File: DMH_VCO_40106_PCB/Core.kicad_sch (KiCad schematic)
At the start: 58 parts, among them Q1 BC558, Q2 BC548, U1 40106, U2 TL074, U3 TL074, U4 TL074

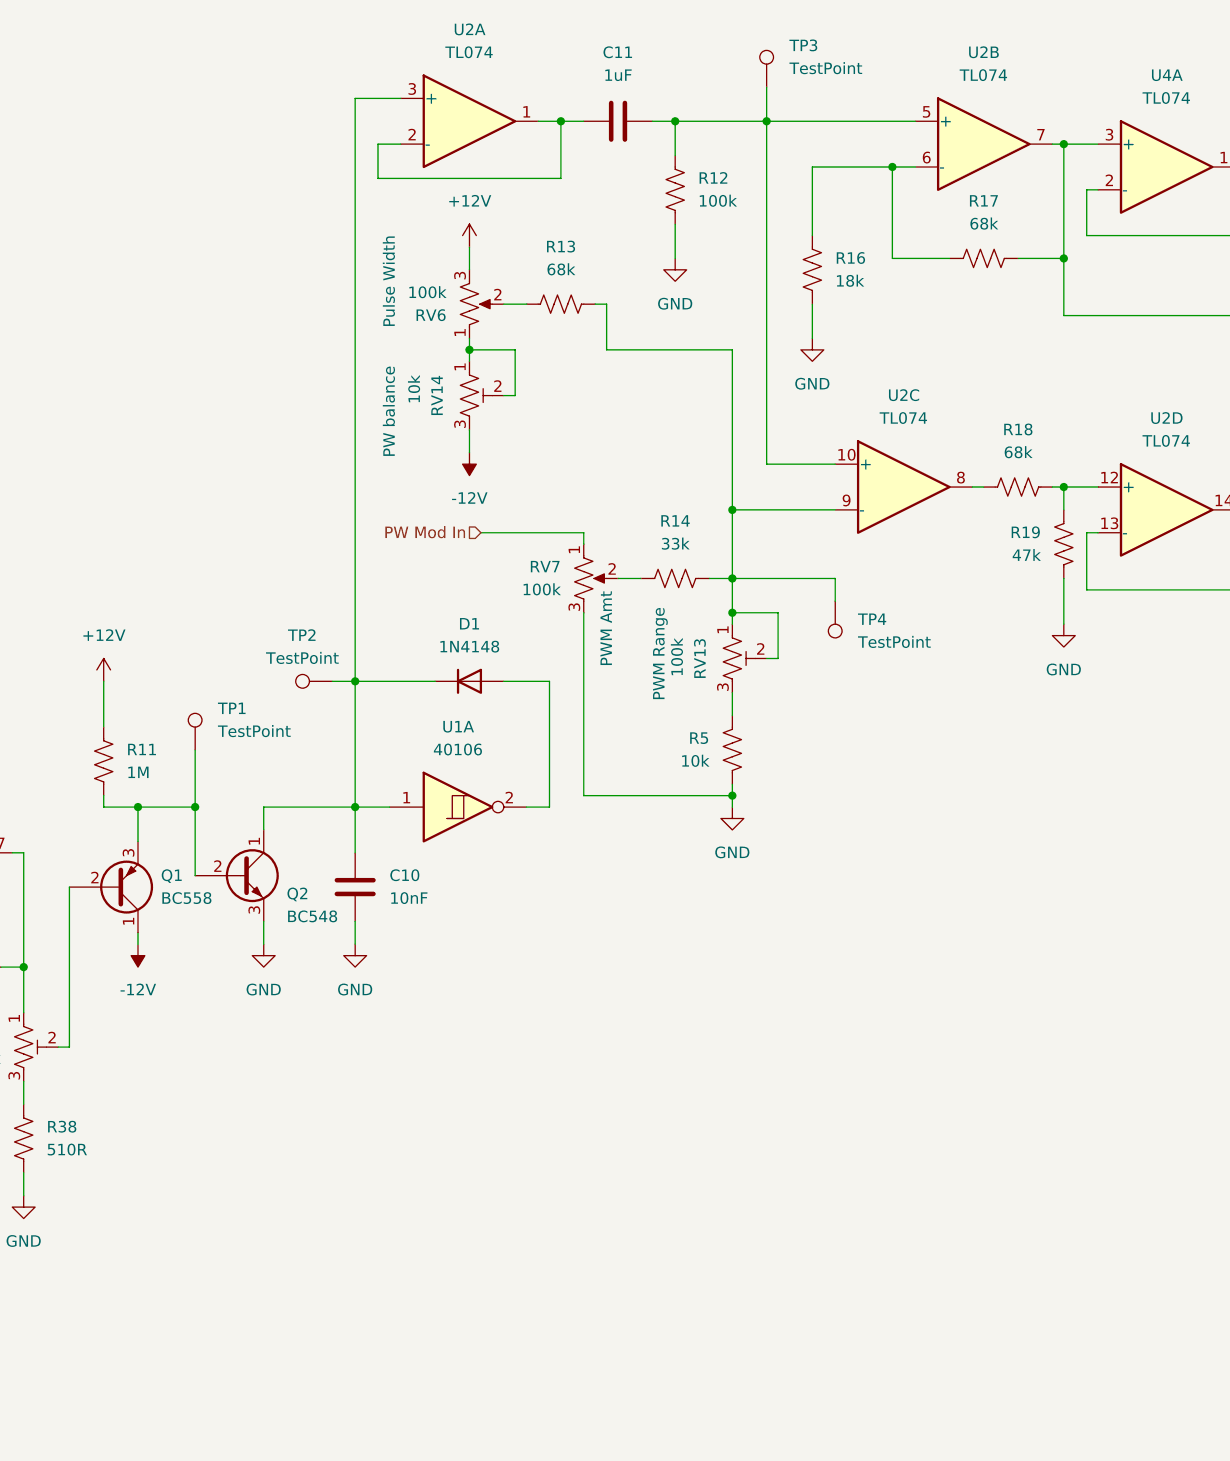
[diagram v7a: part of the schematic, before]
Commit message: Added sawtooth zero crossing pulse generator
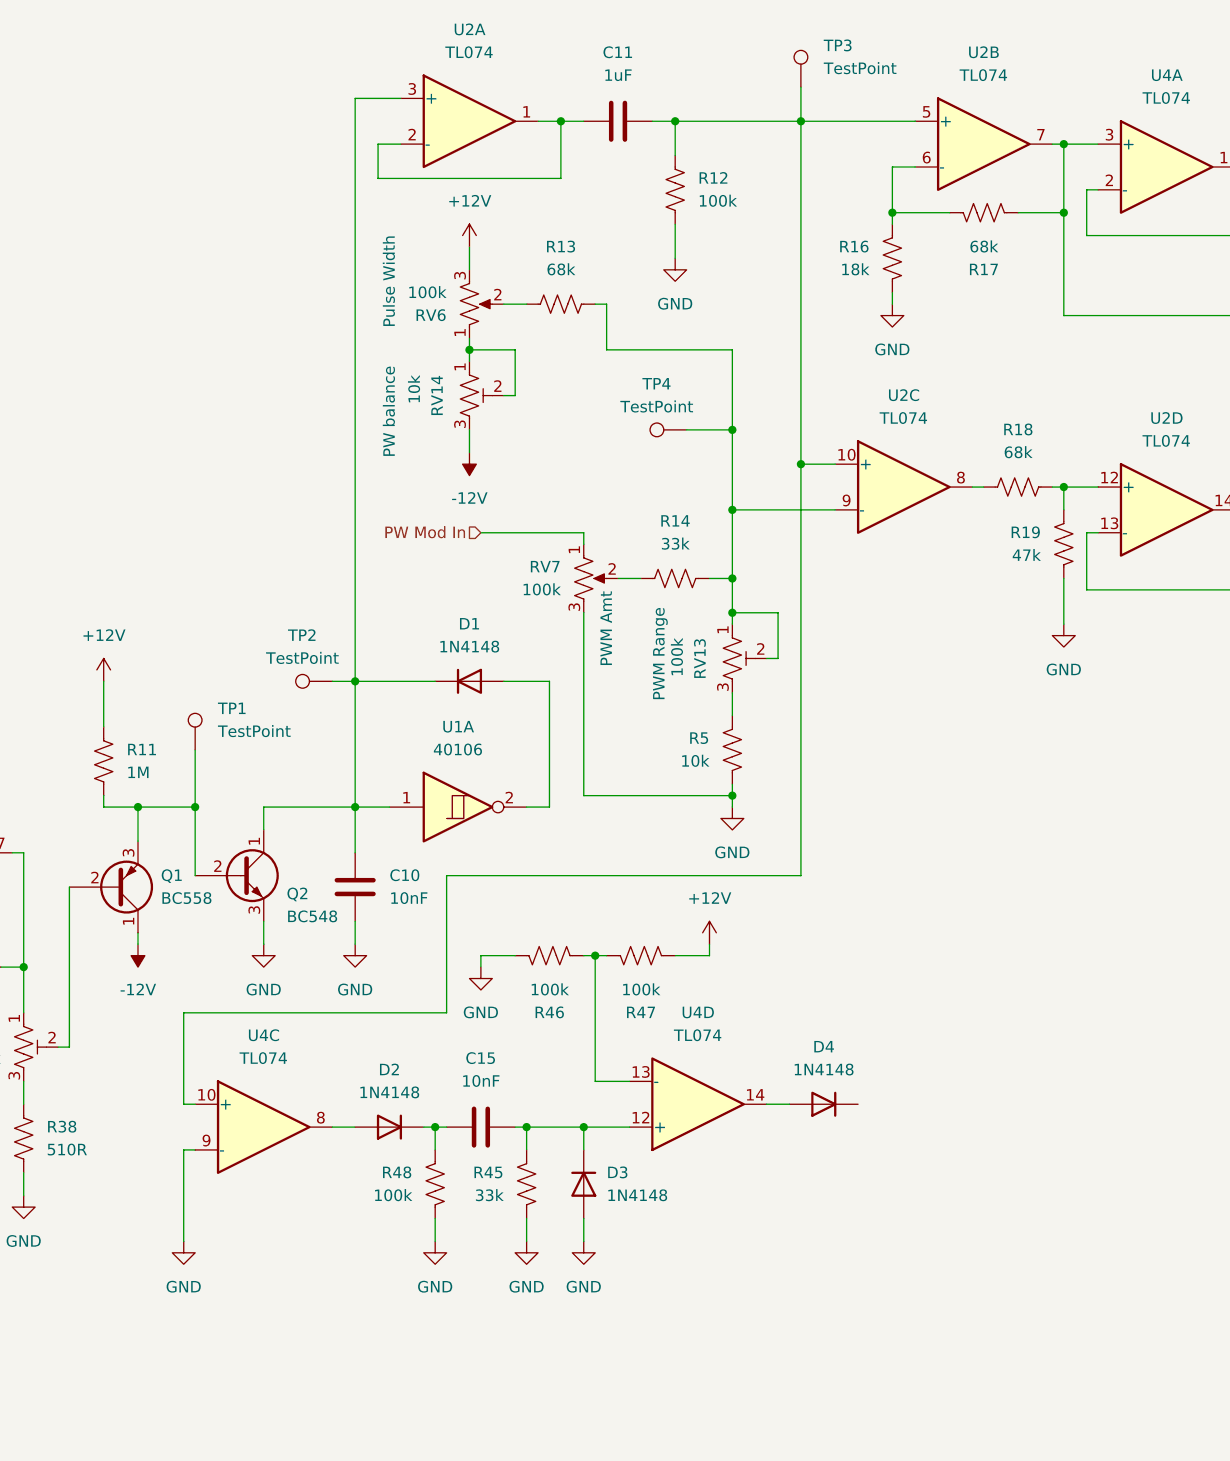
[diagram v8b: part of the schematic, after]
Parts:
- added C15: 10nF, symbol Device:C
- added D2, D3, D4: 1N4148, Diode_THT:D_DO-35_SOD27_P7.62mm_Horizontal, symbol Diode:1N4148
- added R45: 33k, Resistor_THT:R_Axial_DIN0204_L3.6mm_D1.6mm_P5.08mm_Horizontal, symbol Device:R_US
- added R46, R47, R48: 100k, Resistor_THT:R_Axial_DIN0204_L3.6mm_D1.6mm_P5.08mm_Horizontal, symbol Device:R_US
- added unit 3 of U4
- added unit 4 of U4
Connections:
- net +12V: now also R47.2
- net GND: now also D3.2 (A), R45.2, R46.1, R48.2, U4.9 (-)
- net at C11.2, R12.2, TP3.1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: now also U4.10 (+)
- new net: R46.2, R47.1, U4.13 (-)
- new net: D2.2 (A), U4.8
- new net: C15.2, D3.1 (K), R45.1, U4.12 (+)
- new net: D4.2 (A), U4.14
- new net: C15.1, D2.1 (K), R48.1
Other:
- moved on the sheet: R16, R17, TP3, TP4
